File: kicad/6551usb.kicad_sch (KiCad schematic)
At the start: 41 parts, among them J1 Conn_01x03_Male, P1 DLP-USB245R, SW1 SW_DIP_x06, U1 74LS04, U10 74LS74, U11 74LS86, U12 74LS33, U13 74LS273, U14 74LS374, U15 74LS244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

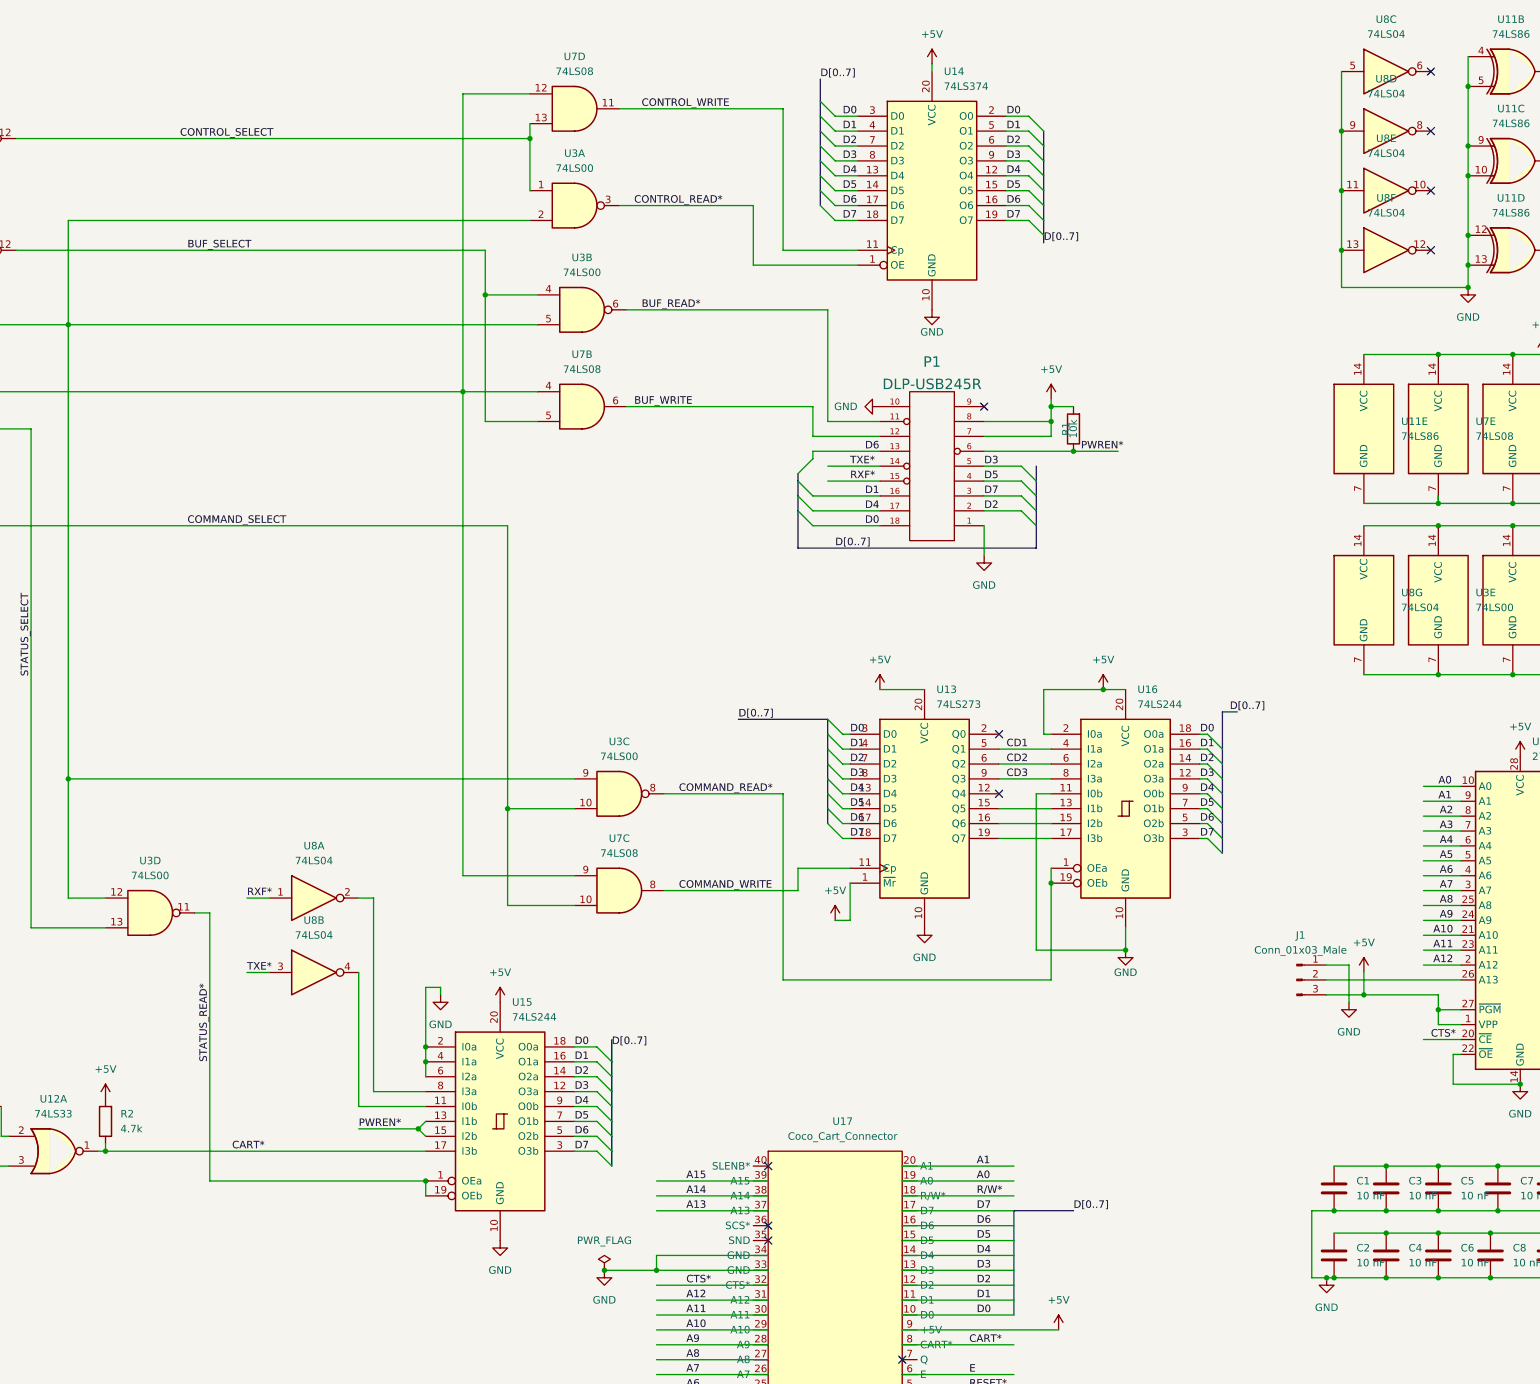
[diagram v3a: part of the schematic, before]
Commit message: Updated to 1.03 to fix interrupt in status register and extend board to full size
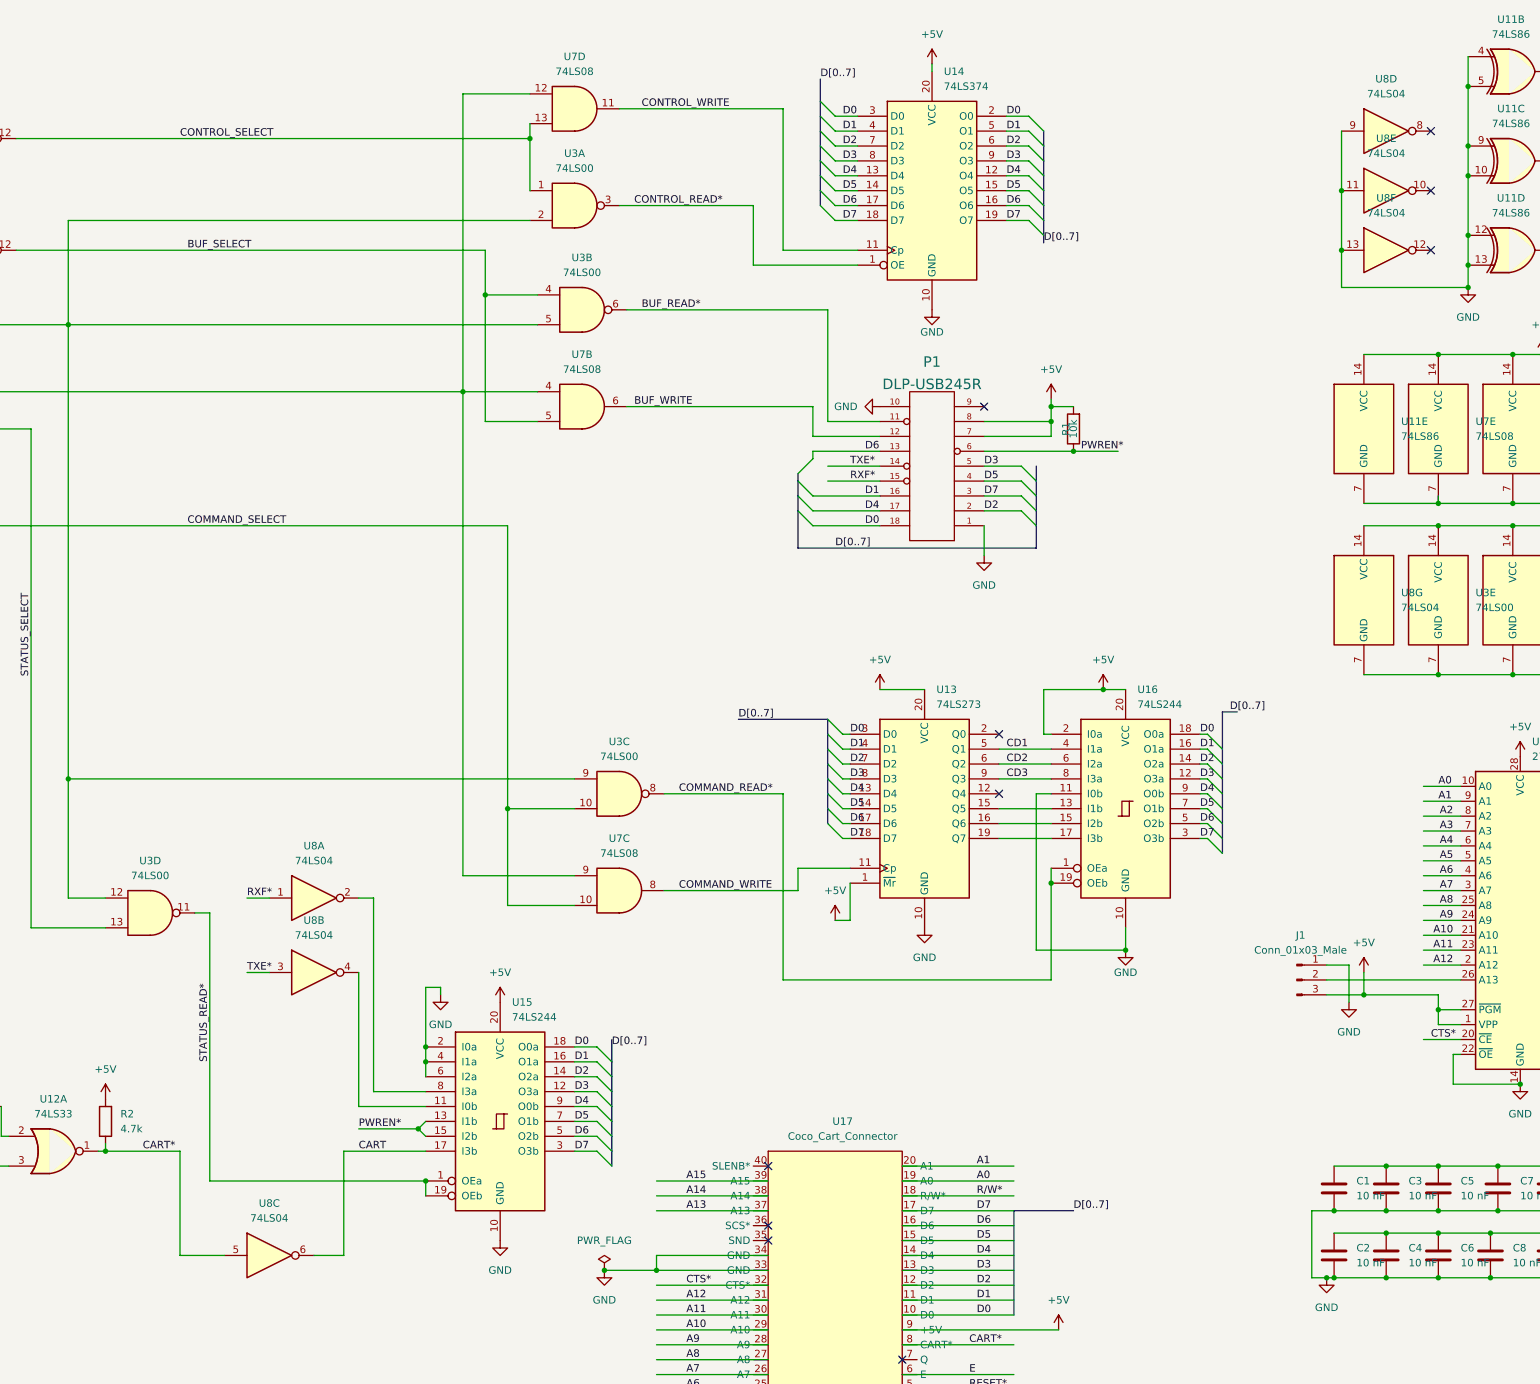
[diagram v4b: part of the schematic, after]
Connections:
- net CART*: now also U8.5; no longer U15.17 (I3b)
- net GND: no longer U8.5
- net CART: now reaches U8.6
- net CART: now also U15.17 (I3b)
- no-connect marks 22 -> 21
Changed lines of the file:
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@@
     (title "CoCo USB Serial")
     (date "2022-11-23")
-    (rev "1.02")
+    (rev "1.03")
   )
   (junction (at 31.75 66.04) (diameter 0) (color 0 0 0 0)
@@
   (junction (at 406.4 209.55) (diameter 0) (color 0 0 0 0)
   )
-  (junction (at 346.71 33.02) (diameter 0) (color 0 0 0 0)
-  )
   (junction (at 406.4 217.17) (diameter 0) (color 0 0 0 0)
   )
@@
   (junction (at 36.83 153.67) (diameter 0) (color 0 0 0 0)
   )
-  (junction (at 135.89 207.01) (diameter 0) (color 0 0 0 0)
-  )
   (junction (at 346.71 53.34) (diameter 0) (color 0 0 0 0)
   )
@@
   (junction (at 36.83 158.75) (diameter 0) (color 0 0 0 0)
   )
+  (junction (at 135.89 207.01) (diameter 0) (color 0 0 0 0)
+  )
   (junction (at 189.23 203.2) (diameter 0) (color 0 0 0 0)
   )
@@
   (no_connect (at 271.78 257.81))
   (no_connect (at 60.96 223.52))
-  (no_connect (at 361.95 22.86))
   (no_connect (at 361.95 53.34))
   (no_connect (at 361.95 33.02))
@@
     (stroke (width 0) (type default) (color 0 0 0 0))
   )
+  (wire (pts (xy 148.59 224.79) (xy 156.21 224.79))
+    (stroke (width 0) (type default) (color 0 0 0 0))
+  )
   (wire (pts (xy 288.29 143.51) (xy 297.18 143.51))
     (stroke (width 0) (type default) (color 0 0 0 0))
@@
     (stroke (width 0) (type default) (color 0 0 0 0))
   )
+  (wire (pts (xy 176.53 207.01) (xy 190.5 207.01))
+    (stroke (width 0) (type default) (color 0 0 0 0))
+  )
   (wire (pts (xy 406.4 217.17) (xy 412.75 217.17))
     (stroke (width 0) (type default) (color 0 0 0 0))
@@
     (stroke (width 0) (type default) (color 0 0 0 0))
   )
+  (wire (pts (xy 148.59 207.01) (xy 148.59 224.79))
+    (stroke (width 0) (type default) (color 0 0 0 0))
+  )
   (wire (pts (xy 200.66 60.96) (xy 209.55 60.96))
     (stroke (width 0) (type default) (color 0 0 0 0))
@@
     (stroke (width 0) (type default) (color 0 0 0 0))
   )
-  (wire (pts (xy 346.71 22.86) (xy 346.71 33.02))
-    (stroke (width 0) (type default) (color 0 0 0 0))
-  )
   (wire (pts (xy 360.68 187.96) (xy 367.03 187.96))
     (stroke (width 0) (type default) (color 0 0 0 0))
@@
     (stroke (width 0) (type default) (color 0 0 0 0))
   )
+  (wire (pts (xy 176.53 224.79) (xy 176.53 207.01))
+    (stroke (width 0) (type default) (color 0 0 0 0))
+  )
   (wire (pts (xy 80.01 196.85) (xy 83.82 196.85))
     (stroke (width 0) (type default) (color 0 0 0 0))
@@
     (stroke (width 0) (type default) (color 0 0 0 0))
   )
+  (wire (pts (xy 171.45 224.79) (xy 176.53 224.79))
+    (stroke (width 0) (type default) (color 0 0 0 0))
+  )
   (wire (pts (xy 346.71 59.69) (xy 368.3 59.69))
     (stroke (width 0) (type default) (color 0 0 0 0))
@@
     (stroke (width 0) (type default) (color 0 0 0 0))
   )
+  (wire (pts (xy 135.89 207.01) (xy 148.59 207.01))
+    (stroke (width 0) (type default) (color 0 0 0 0))
+  )
   (wire (pts (xy 26.67 19.05) (xy 26.67 31.75))
     (stroke (width 0) (type default) (color 0 0 0 0))
@@
     (stroke (width 0) (type default) (color 0 0 0 0))
   )
-  (wire (pts (xy 135.89 207.01) (xy 190.5 207.01))
-    (stroke (width 0) (type default) (color 0 0 0 0))
-  )
   (wire (pts (xy 260.35 30.48) (xy 264.16 30.48))
     (stroke (width 0) (type default) (color 0 0 0 0))
@@
     (effects (font (size 1.27 1.27)) (justify left bottom))
   )
-  (label "CART*" (at 157.48 207.01 0)
+  (label "CART*" (at 142.24 207.01 0)
     (effects (font (size 1.27 1.27)) (justify left bottom))
   )
@@
     (effects (font (size 1.27 1.27)) (justify left bottom))
   )
+  (label "CART" (at 179.07 207.01 0)
+    (effects (font (size 1.27 1.27)) (justify left bottom))
+  )
   (label "D7" (at 261.62 48.26 0)
     (effects (font (size 1.27 1.27)) (justify left bottom))
@@
     (pin "7")
   )
+  (symbol (lib_id "74xx:74LS04") (at 163.83 224.79 0) (unit 3)
+    (in_bom yes) (on_board yes) (fields_autoplaced)
+    (property "Reference" "U8" (id 0) (at 163.83 215.9 0))
+    (property "Value" "74LS04" (id 1) (at 163.83 218.44 0))
+    (property "Footprint" "Package_DIP:DIP-14_W7.62mm" (id 2) (at 163.83 224.79 0)
+      (effects (font (size 1.27 1.27)) hide)
+    )
+    (property "Datasheet" "http://www.ti.com/lit/gpn/sn74LS04" (id 3) (at 163.83 224.79 0)
+      (effects (font (size 1.27 1.27)) hide)
+    )
+    (pin "1")
+    (pin "2")
+    (pin "3")
+    (pin "4")
+    (pin "5")
+    (pin "6")
+    (pin "8")
+    (pin "9")
+    (pin "10")
+    (pin "11")
+    (pin "12")
+    (pin "13")
+    (pin "14")
+    (pin "7")
+  )
   (symbol (lib_id "power:+5V") (at 267.97 128.27 0) (unit 1)
     (in_bom yes) (on_board yes) (fields_autoplaced)
@@
     (pin "2")
   )
-  (symbol (lib_id "74xx:74LS04") (at 354.33 22.86 0) (unit 3)
-    (in_bom yes) (on_board yes) (fields_autoplaced)
-    (property "Reference" "U8" (id 0) (at 354.33 13.97 0))
-    (property "Value" "74LS04" (id 1) (at 354.33 16.51 0))
-    (property "Footprint" "Package_DIP:DIP-14_W7.62mm" (id 2) (at 354.33 22.86 0)
-      (effects (font (size 1.27 1.27)) hide)
-    )
-    (property "Datasheet" "http://www.ti.com/lit/gpn/sn74LS04" (id 3) (at 354.33 22.86 0)
-      (effects (font (size 1.27 1.27)) hide)
-    )
-    (pin "1")
-    (pin "2")
-    (pin "3")
-    (pin "4")
-    (pin "5")
-    (pin "6")
-    (pin "8")
-    (pin "9")
-    (pin "10")
-    (pin "11")
-    (pin "12")
-    (pin "13")
-    (pin "14")
-    (pin "7")
-  )
   (symbol (lib_id "Device:C") (at 345.44 213.36 0) (unit 1)
     (in_bom yes) (on_board yes) (fields_autoplaced)
@@
       (reference "U8") (unit 2) (value "74LS04") (footprint "Package_DIP:DIP-14_W7.62mm")
     )
-    (path "/8f25e03c-1226-42c5-8f1e-aeeb8ff0cec2"
+    (path "/8212497f-5c01-4fbd-9093-b7d33081e0c7"
       (reference "U8") (unit 3) (value "74LS04") (footprint "Package_DIP:DIP-14_W7.62mm")
     )

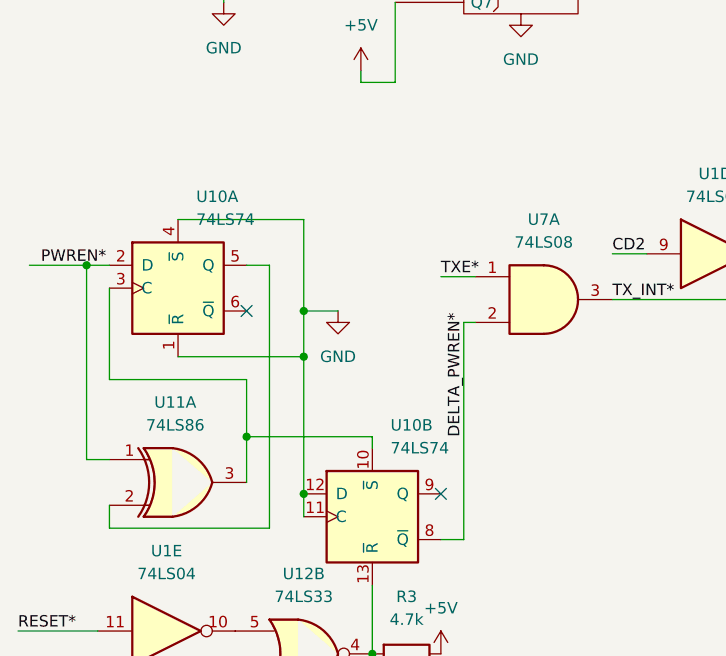
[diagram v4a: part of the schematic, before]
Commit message: fixed fab files in kicad folder
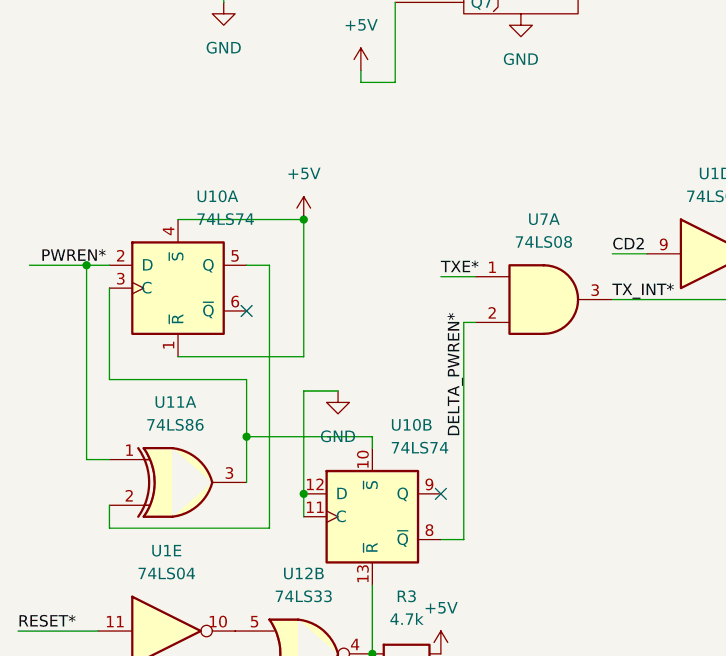
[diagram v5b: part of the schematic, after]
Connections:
- net +5V: now also U10.1 (~{R}), U10.4 (~{S})
- net GND: no longer U10.1 (~{R}), U10.4 (~{S})
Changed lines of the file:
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@@
   (title_block
     (title "CoCo USB Serial")
-    (date "2022-11-23")
-    (rev "1.03")
+    (date "2022-11-25")
+    (rev "1.04")
   )
   (junction (at 31.75 66.04) (diameter 0) (color 0 0 0 0)
@@
   (junction (at 368.3 25.4) (diameter 0) (color 0 0 0 0)
   )
-  (junction (at 45.72 203.2) (diameter 0) (color 0 0 0 0)
-  )
   (junction (at 345.44 228.6) (diameter 0) (color 0 0 0 0)
   )
@@
   (junction (at 363.22 220.98) (diameter 0) (color 0 0 0 0)
   )
-  (junction (at 45.72 208.28) (diameter 0) (color 0 0 0 0)
-  )
   (junction (at 87.63 86.36) (diameter 0) (color 0 0 0 0)
   )
@@
   (junction (at 388.62 125.73) (diameter 0) (color 0 0 0 0)
   )
+  (junction (at 45.72 193.04) (diameter 0) (color 0 0 0 0)
+  )
   (junction (at 300.99 87.63) (diameter 0) (color 0 0 0 0)
   )
@@
     (stroke (width 0) (type default) (color 0 0 0 0))
   )
-  (wire (pts (xy 45.72 208.28) (xy 45.72 203.2))
+  (wire (pts (xy 45.72 193.04) (xy 45.72 208.28))
     (stroke (width 0) (type default) (color 0 0 0 0))
   )
@@
     (stroke (width 0) (type default) (color 0 0 0 0))
   )
-  (wire (pts (xy 45.72 203.2) (xy 49.53 203.2))
+  (wire (pts (xy 45.72 212.09) (xy 49.53 212.09))
     (stroke (width 0) (type default) (color 0 0 0 0))
   )
@@
     (stroke (width 0) (type default) (color 0 0 0 0))
   )
-  (wire (pts (xy 45.72 223.52) (xy 45.72 208.28))
+  (wire (pts (xy 45.72 223.52) (xy 45.72 212.09))
     (stroke (width 0) (type default) (color 0 0 0 0))
   )
@@
     (stroke (width 0) (type default) (color 0 0 0 0))
   )
-  (wire (pts (xy 45.72 193.04) (xy 45.72 203.2))
-    (stroke (width 0) (type default) (color 0 0 0 0))
-  )
   (wire (pts (xy 264.16 55.88) (xy 246.38 55.88))
     (stroke (width 0) (type default) (color 0 0 0 0))
@@
     (pin "7")
   )
-  (symbol (lib_id "power:GND") (at 49.53 203.2 0) (unit 1)
+  (symbol (lib_id "power:GND") (at 49.53 212.09 0) (unit 1)
     (in_bom yes) (on_board yes) (fields_autoplaced)
-    (property "Reference" "#PWR04" (id 0) (at 49.53 209.55 0)
+    (property "Reference" "#PWR04" (id 0) (at 49.53 218.44 0)
       (effects (font (size 1.27 1.27)) hide)
     )
-    (property "Value" "GND" (id 1) (at 49.53 208.28 0))
-    (property "Footprint" "" (id 2) (at 49.53 203.2 0)
+    (property "Value" "GND" (id 1) (at 49.53 217.17 0))
+    (property "Footprint" "" (id 2) (at 49.53 212.09 0)
       (effects (font (size 1.27 1.27)) hide)
     )
-    (property "Datasheet" "" (id 3) (at 49.53 203.2 0)
+    (property "Datasheet" "" (id 3) (at 49.53 212.09 0)
       (effects (font (size 1.27 1.27)) hide)
     )
@@
     (pin "7")
   )
+  (symbol (lib_id "power:+5V") (at 45.72 193.04 0) (unit 1)
+    (in_bom yes) (on_board yes) (fields_autoplaced)
+    (property "Reference" "#PWR?" (id 0) (at 45.72 196.85 0)
+      (effects (font (size 1.27 1.27)) hide)
+    )
+    (property "Value" "+5V" (id 1) (at 45.72 187.96 0))
+    (property "Footprint" "" (id 2) (at 45.72 193.04 0)
+      (effects (font (size 1.27 1.27)) hide)
+    )
+    (property "Datasheet" "" (id 3) (at 45.72 193.04 0)
+      (effects (font (size 1.27 1.27)) hide)
+    )
+    (pin "1")
+  )
   (symbol (lib_id "74xx:74LS33") (at 127 207.01 0) (unit 1)
     (in_bom yes) (on_board yes) (fields_autoplaced)
@@
       (reference "#PWR0129") (unit 1) (value "+5V") (footprint "")
     )
+    (path "/513125ae-da41-4e42-a192-a4b760568210"
+      (reference "#PWR?") (unit 1) (value "+5V") (footprint "")
+    )
     (path "/92900cd0-548c-482b-a1b2-9ce27355b8a5"
